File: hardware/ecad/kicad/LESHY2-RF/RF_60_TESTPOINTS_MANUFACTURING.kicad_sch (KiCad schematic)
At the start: 0 parts

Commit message: complete exact H2.3.13 RF testpoint sheet
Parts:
- added TP1: TP_PACK_FIXTURE_3V3, TestPoint:TestPoint_Pad_D1.0mm, symbol Leshy2:RF60_TP_PACK_FIXTURE_3V3
- added TP10: TP_EVIDENCE_MASK_INT_N, TestPoint:TestPoint_Pad_D1.0mm, symbol Leshy2:RF60_TP_EVIDENCE_MASK_INT_N
- added TP11: TP_SAFETY_UART_TX, TestPoint:TestPoint_Pad_D1.0mm, symbol Leshy2:RF60_TP_SAFETY_UART_TX
- added TP12: TP_SAFETY_UART_RX, TestPoint:TestPoint_Pad_D1.0mm, symbol Leshy2:RF60_TP_SAFETY_UART_RX
- added TP13: TP_SAFETY_SWDIO, TestPoint:TestPoint_Pad_D1.0mm, symbol Leshy2:RF60_TP_SAFETY_SWDIO
- added TP14: TP_SAFETY_SWCLK, TestPoint:TestPoint_Pad_D1.0mm, symbol Leshy2:RF60_TP_SAFETY_SWCLK
- added TP15: TP_SAFETY_NRST, TestPoint:TestPoint_Pad_D1.0mm, symbol Leshy2:RF60_TP_SAFETY_NRST
- added TP16: TP_EV_N2, TestPoint:TestPoint_Pad_D1.0mm, symbol Leshy2:RF60_TP_EV_N2
- added TP17: TP_EV_N3, TestPoint:TestPoint_Pad_D1.0mm, symbol Leshy2:RF60_TP_EV_N3
- added TP18: TP_EV_N4, TestPoint:TestPoint_Pad_D1.0mm, symbol Leshy2:RF60_TP_EV_N4
- added TP19: TP_EV_N5, TestPoint:TestPoint_Pad_D1.0mm, symbol Leshy2:RF60_TP_EV_N5
- added TP2: TP_PACK_UART_TX, TestPoint:TestPoint_Pad_D1.0mm, symbol Leshy2:RF60_TP_PACK_UART_TX
- added TP20: TP_EV_N6, TestPoint:TestPoint_Pad_D1.0mm, symbol Leshy2:RF60_TP_EV_N6
- added TP21: TP_EV_N8, TestPoint:TestPoint_Pad_D1.0mm, symbol Leshy2:RF60_TP_EV_N8
- added TP22: TP_ANY_TX_AON_N, TestPoint:TestPoint_Pad_D1.0mm, symbol Leshy2:RF60_TP_ANY_TX_AON_N
- added TP23: TP_POWER_TEMP, TestPoint:TestPoint_Pad_D1.0mm, symbol Leshy2:RF60_TP_POWER_TEMP
- added TP24: TP_RF_TEMP, TestPoint:TestPoint_Pad_D1.0mm, symbol Leshy2:RF60_TP_RF_TEMP
- added TP25: TP_RP_RESET_N, TestPoint:TestPoint_Pad_D1.0mm, symbol Leshy2:RF60_TP_RP_RESET_N
- added TP26: TP_RUN_PERMIT, TestPoint:TestPoint_Pad_D1.0mm, symbol Leshy2:RF60_TP_RUN_PERMIT
- added TP27: TP_POWER_FAULT_N, TestPoint:TestPoint_Pad_D1.0mm, symbol Leshy2:RF60_TP_POWER_FAULT_N
- added TP28: TP_POWER_GROUND, TestPoint:TestPoint_Pad_D1.0mm, symbol Leshy2:RF60_TP_POWER_GROUND
- added TP29: TP_AON_SAFE_3V3, TestPoint:TestPoint_Pad_D1.0mm, symbol Leshy2:RF60_TP_AON_SAFE_3V3
- added TP3: TP_PACK_UART_RX, TestPoint:TestPoint_Pad_D1.0mm, symbol Leshy2:RF60_TP_PACK_UART_RX
- added TP30: TP_3V3_MAIN, TestPoint:TestPoint_Pad_D1.0mm, symbol Leshy2:RF60_TP_3V3_MAIN
- added TP4: TP_PACK_SWDIO, TestPoint:TestPoint_Pad_D1.0mm, symbol Leshy2:RF60_TP_PACK_SWDIO
- added TP5: TP_PACK_SWCLK, TestPoint:TestPoint_Pad_D1.0mm, symbol Leshy2:RF60_TP_PACK_SWCLK
- added TP6: TP_PACK_NRST, TestPoint:TestPoint_Pad_D1.0mm, symbol Leshy2:RF60_TP_PACK_NRST
- added TP7: TP_MAIN_RAW_PG_N, TestPoint:TestPoint_Pad_D1.0mm, symbol Leshy2:RF60_TP_MAIN_RAW_PG_N
- added TP8: TP_VOICE_UPDATE, TestPoint:TestPoint_Pad_D1.0mm, symbol Leshy2:RF60_TP_VOICE_UPDATE
- added TP9: TP_VOICE_RAW_PG_N, TestPoint:TestPoint_Pad_D1.0mm, symbol Leshy2:RF60_TP_VOICE_RAW_PG_N
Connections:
- new net 3V3_MAIN: TP30.1 (TEST)
- new net ANY_TX_AON_N: TP22.1 (TEST)
- new net AON_SAFE_3V3: TP29.1 (TEST)
- new net EVIDENCE_MASK_INT_N_TP: TP10.1 (TEST)
- new net EV_N2_NRF0: TP16.1 (TEST)
- new net EV_N3_NRF1: TP17.1 (TEST)
- new net EV_N4_NRF2: TP18.1 (TEST)
- new net EV_N5_CC: TP19.1 (TEST)
- new net EV_N6_VOICE: TP20.1 (TEST)
- new net EV_N8_LORA_EXT: TP21.1 (TEST)
- new net MAIN_RAW_3V3_PG_N: TP7.1 (TEST)
- new net PACK_ADMISSION_NRST_N: TP6.1 (TEST)
- new net PACK_ADMISSION_SWCLK: TP5.1 (TEST)
- new net PACK_ADMISSION_SWDIO: TP4.1 (TEST)
- new net PACK_ADMISSION_UART_RX: TP3.1 (TEST)
- new net PACK_ADMISSION_UART_TX: TP2.1 (TEST)
- new net PACK_FIXTURE_3V3: TP1.1 (TEST)
- new net POWER_FAULT_N: TP27.1 (TEST)
- new net POWER_GROUND: TP28.1 (TEST)
- new net POWER_ZONE_TEMP_ADC: TP23.1 (TEST)
- new net RF_ZONE_TEMP_ADC: TP24.1 (TEST)
- new net RP_RESET_N: TP25.1 (TEST)
- new net RUN_PERMIT: TP26.1 (TEST)
- new net SAFETY_CONTROLLER_NRST_N: TP15.1 (TEST)
- new net SAFETY_SERVICE_UART_RX: TP12.1 (TEST)
- new net SAFETY_SERVICE_UART_TX: TP11.1 (TEST)
- new net SAFETY_SWCLK: TP14.1 (TEST)
- new net SAFETY_SWDIO: TP13.1 (TEST)
- new net VOICE_RAW_4V_PG_N: TP9.1 (TEST)
- new net VOICE_UPDATE_FIXTURE: TP8.1 (TEST)
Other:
- title: (none) -> Leshy2 — exact RF/power manufacturing and diagnostic test pads

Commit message: complete H2 schematic review package
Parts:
- added TP60007: TP_SYS_I2C_SDA, TestPoint:TestPoint_Pad_D1.0mm, symbol Leshy2:RF60_TP_SYS_I2C_SDA
- added TP60008: TP_SYS_I2C_SCL, TestPoint:TestPoint_Pad_D1.0mm, symbol Leshy2:RF60_TP_SYS_I2C_SCL
- added TP60009: TP_SYS_INT_N, TestPoint:TestPoint_Pad_D1.0mm, symbol Leshy2:RF60_TP_SYS_INT_N
- added TP60010: TP_PD_LOCAL_I2C_SDA, TestPoint:TestPoint_Pad_D1.0mm, symbol Leshy2:RF60_TP_PD_LOCAL_I2C_SDA
- added TP60011: TP_PD_LOCAL_I2C_SCL, TestPoint:TestPoint_Pad_D1.0mm, symbol Leshy2:RF60_TP_PD_LOCAL_I2C_SCL
- added TP60012: TP_PD_EEPROM_WP, TestPoint:TestPoint_Pad_D1.0mm, symbol Leshy2:RF60_TP_PD_EEPROM_WP
- added TP60013: TP_RP_SERVICE_VBUS_SENSE, TestPoint:TestPoint_Pad_D1.0mm, symbol Leshy2:RF60_TP_RP_SERVICE_VBUS_SENSE
- added TP60038: TP_RUN_LOOP_RAW, TestPoint:TestPoint_Pad_D1.0mm, symbol Leshy2:RF60_TP_RUN_LOOP_RAW
- added TP60039: TP_RUN_EDGE, TestPoint:TestPoint_Pad_D1.0mm, symbol Leshy2:RF60_TP_RUN_EDGE
- added TP60040: TP_FAULT_ASSERT_N, TestPoint:TestPoint_Pad_D1.0mm, symbol Leshy2:RF60_TP_FAULT_ASSERT_N
- added TP60041: TP_WDI, TestPoint:TestPoint_Pad_D1.0mm, symbol Leshy2:RF60_TP_WDI
- added TP60042: TP_POR_N, TestPoint:TestPoint_Pad_D1.0mm, symbol Leshy2:RF60_TP_POR_N
- added TP60043: TP_FAULT_LATCH_SENSE_AON, TestPoint:TestPoint_Pad_D1.0mm, symbol Leshy2:RF60_TP_FAULT_LATCH_SENSE_AON
- added TP60044: TP_NRF0_CE_SAFE, TestPoint:TestPoint_Pad_D1.0mm, symbol Leshy2:RF60_TP_NRF0_CE_SAFE
- added TP60045: TP_NRF1_CE_SAFE, TestPoint:TestPoint_Pad_D1.0mm, symbol Leshy2:RF60_TP_NRF1_CE_SAFE
- added TP60046: TP_NRF2_CE_SAFE, TestPoint:TestPoint_Pad_D1.0mm, symbol Leshy2:RF60_TP_NRF2_CE_SAFE
- added TP60047: TP_NRF_RAIL_EN_SAFE, TestPoint:TestPoint_Pad_D1.0mm, symbol Leshy2:RF60_TP_NRF_RAIL_EN_SAFE
- added TP60048: TP_CC_RAIL_EN_SAFE, TestPoint:TestPoint_Pad_D1.0mm, symbol Leshy2:RF60_TP_CC_RAIL_EN_SAFE
- added TP60049: TP_VOICE_RAIL_EN_SAFE, TestPoint:TestPoint_Pad_D1.0mm, symbol Leshy2:RF60_TP_VOICE_RAIL_EN_SAFE
- added TP60050: TP_VOICE_PTT_SAFE_N, TestPoint:TestPoint_Pad_D1.0mm, symbol Leshy2:RF60_TP_VOICE_PTT_SAFE_N
- added TP60051: TP_EXT_5V_EN_SAFE, TestPoint:TestPoint_Pad_D1.0mm, symbol Leshy2:RF60_TP_EXT_5V_EN_SAFE
- added TP60052: TP_RP_ANY_TX_N, TestPoint:TestPoint_Pad_D1.0mm, symbol Leshy2:RF60_TP_RP_ANY_TX_N
- renumbered TP1 to TP60001, TP2 to TP60002, TP3 to TP60003, TP4 to TP60004, TP5 to TP60005, TP6 to TP60006, TP7 to TP60014, TP8 to TP60015, TP9 to TP60016, TP10 to TP60017, TP11 to TP60018, TP12 to TP60019, TP13 to TP60020, TP14 to TP60021, TP15 to TP60022, TP16 to TP60023, TP17 to TP60024, TP18 to TP60025, TP19 to TP60026, TP20 to TP60027, TP21 to TP60028, TP22 to TP60029, TP23 to TP60030, TP24 to TP60031, TP25 to TP60032, TP26 to TP60033, TP27 to TP60034, TP28 to TP60035, TP29 to TP60036, TP30 to TP60037
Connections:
- new net CC_PWR_EN_SAFE: TP60048.1 (TEST)
- new net EXT_ANY_5V_EN_SAFE: TP60051.1 (TEST)
- new net FAULT_ASSERT_N: TP60040.1 (TEST)
- new net FAULT_LATCH_SENSE_AON: TP60043.1 (TEST)
- new net NRF0_CE_SAFE: TP60044.1 (TEST)
- new net NRF1_CE_SAFE: TP60045.1 (TEST)
- new net NRF2_CE_SAFE: TP60046.1 (TEST)
- new net NRF_GROUP_PWR_EN_SAFE: TP60047.1 (TEST)
- new net PD_EEPROM_WP: TP60012.1 (TEST)
- new net PD_LOCAL_I2C_SCL: TP60011.1 (TEST)
- new net PD_LOCAL_I2C_SDA: TP60010.1 (TEST)
- new net POR_N: TP60042.1 (TEST)
- new net RP_ANY_TX_N: TP60052.1 (TEST)
- new net RP_SERVICE_VBUS_SENSE_ONLY: TP60013.1 (TEST)
- new net RUN_EDGE: TP60039.1 (TEST)
- new net RUN_LOOP_RAW: TP60038.1 (TEST)
- new net SAFETY_WATCHDOG_WDI: TP60041.1 (TEST)
- new net SYS_I2C_SCL: TP60008.1 (TEST)
- new net SYS_I2C_SDA: TP60007.1 (TEST)
- new net SYS_INT_N: TP60009.1 (TEST)
- new net VOICE_DOMAIN_EN_SAFE: TP60049.1 (TEST)
- new net VOICE_PTT_SAFE_N: TP60050.1 (TEST)
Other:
- moved on the sheet: TP60014, TP60015, TP60016, TP60017, TP60018, TP60019, TP60020, TP60021, TP60022, TP60023, TP60024, TP60025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

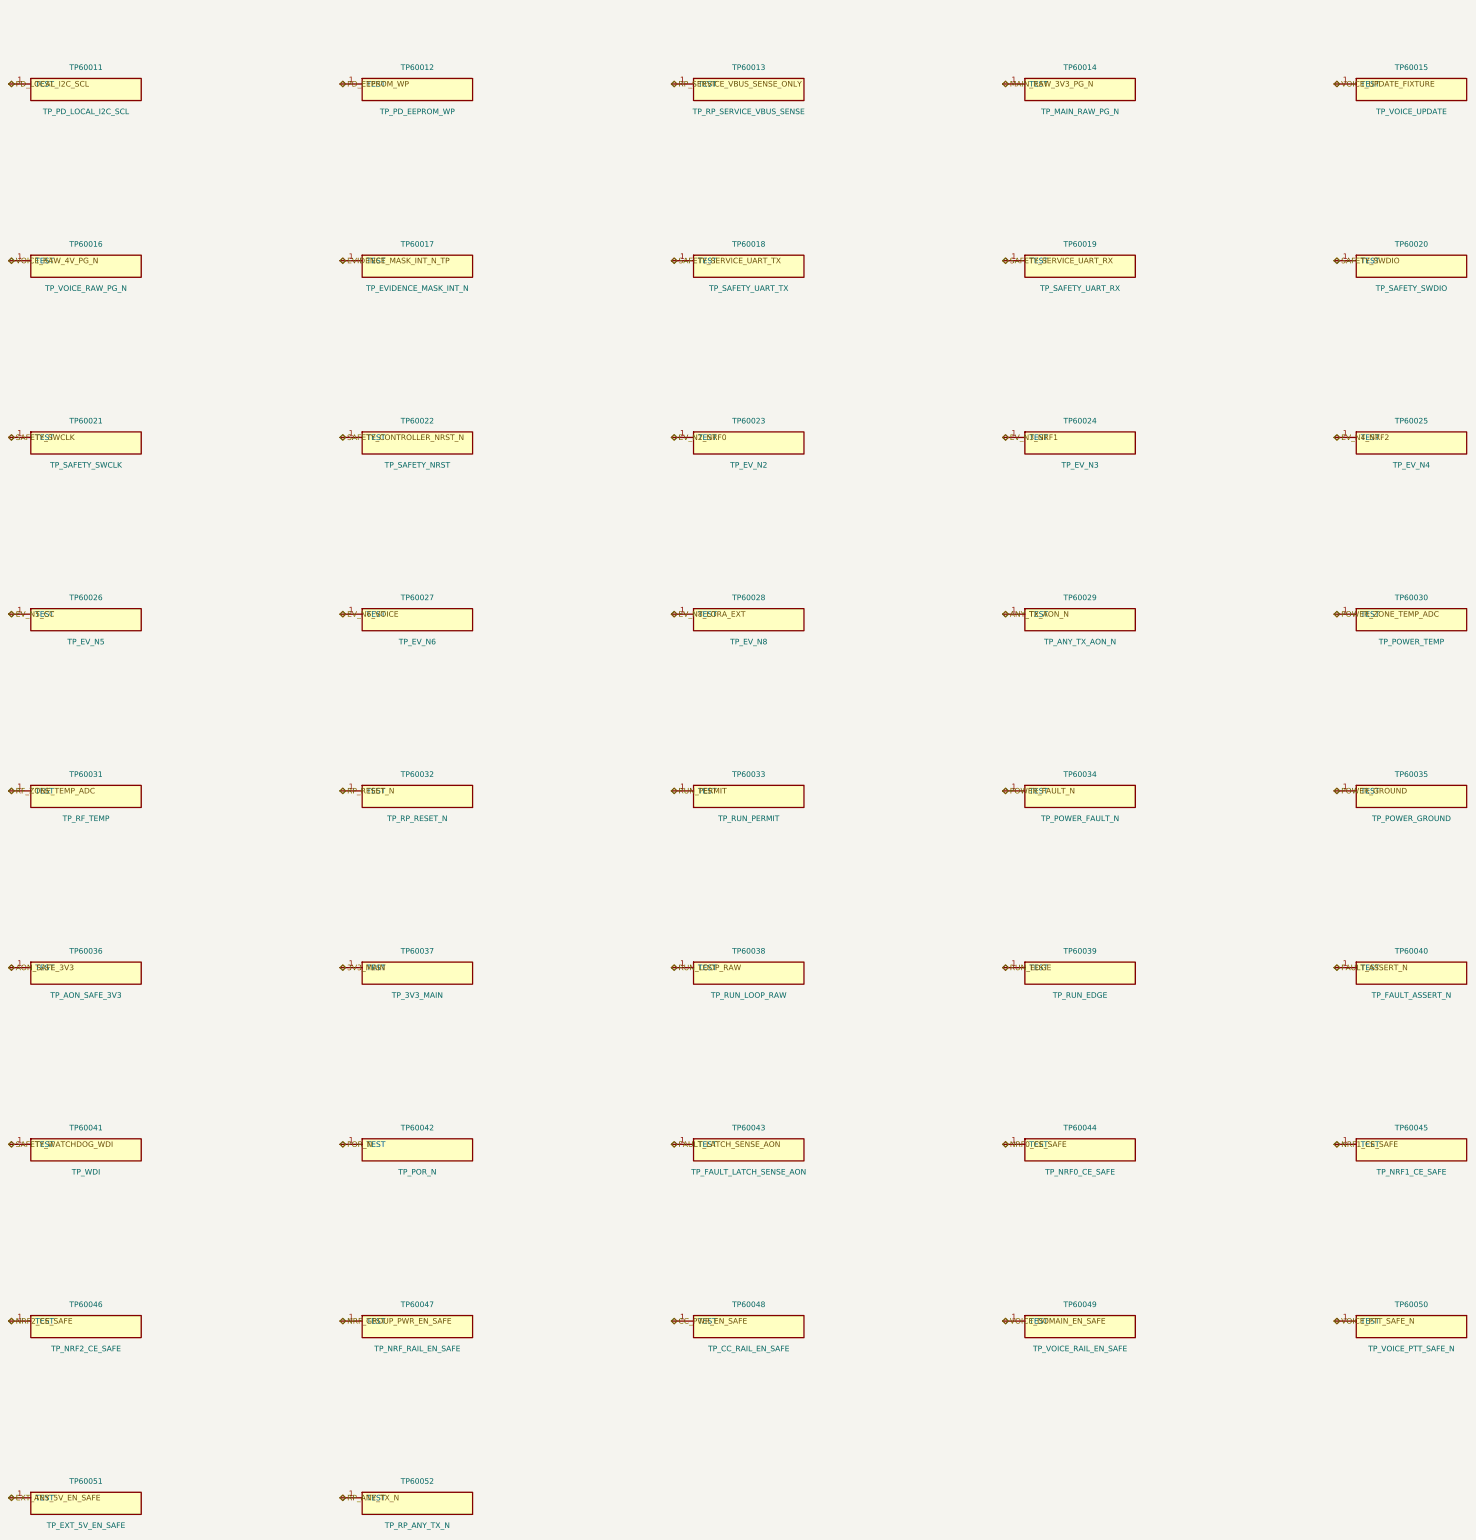
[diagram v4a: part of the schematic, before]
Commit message: Reclose H2 through H4 on dual SA818S architecture
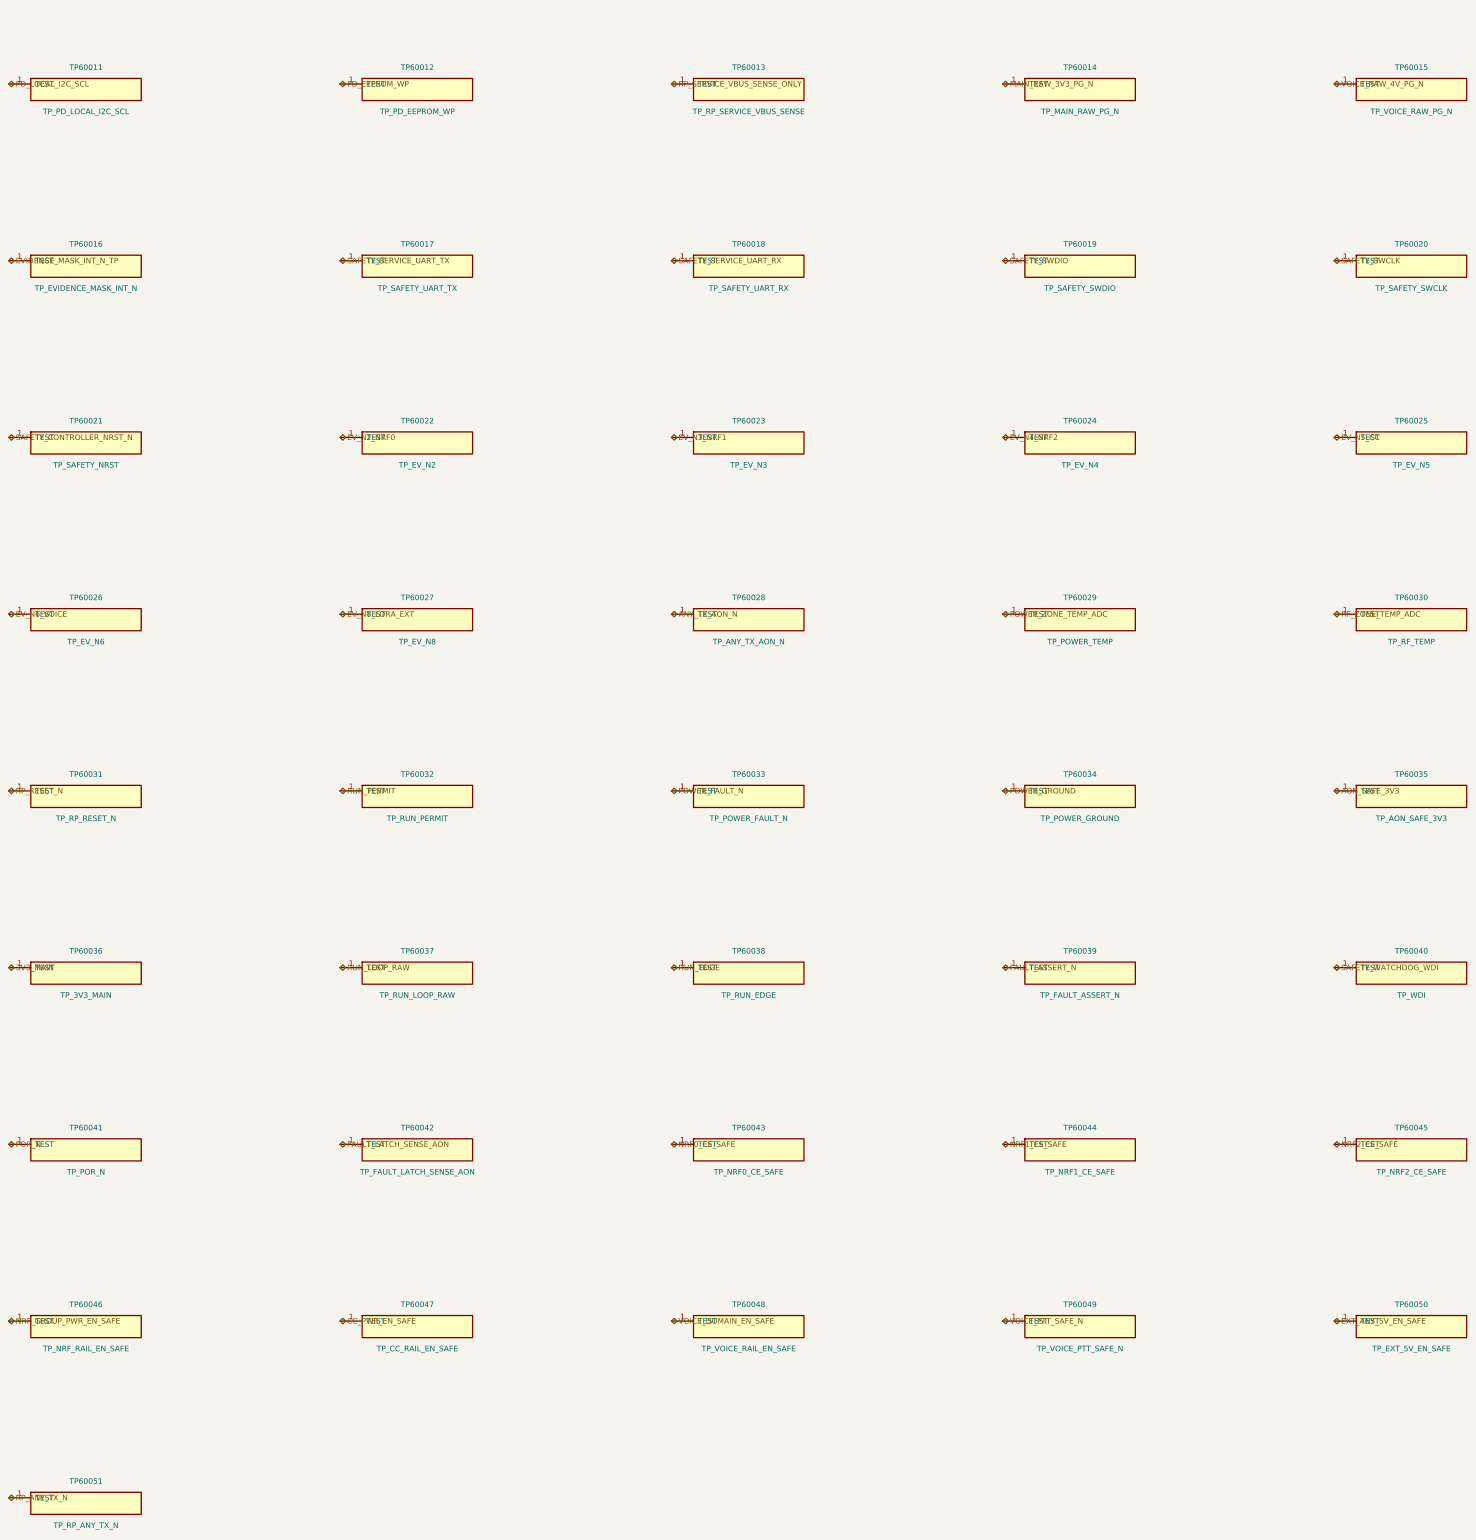
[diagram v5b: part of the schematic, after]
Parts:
- removed TP60015: TP_VOICE_UPDATE, TestPoint:TestPoint_Pad_D1.0mm, symbol Leshy2:RF60_TP_VOICE_UPDATE
- renumbered TP60016 to TP60015, TP60017 to TP60016, TP60018 to TP60017, TP60019 to TP60018, TP60020 to TP60019, TP60021 to TP60020, TP60022 to TP60021, TP60023 to TP60022, TP60024 to TP60023, TP60025 to TP60024, TP60026 to TP60025, TP60027 to TP60026, TP60028 to TP60027, TP60029 to TP60028, TP60030 to TP60029, TP60031 to TP60030, TP60032 to TP60031, TP60033 to TP60032, TP60034 to TP60033, TP60035 to TP60034, TP60036 to TP60035, TP60037 to TP60036, TP60038 to TP60037, TP60039 to TP60038, TP60040 to TP60039, TP60041 to TP60040, TP60042 to TP60041, TP60043 to TP60042, TP60044 to TP60043, TP60045 to TP60044, TP60046 to TP60045, TP60047 to TP60046, TP60048 to TP60047, TP60049 to TP60048, TP60050 to TP60049, TP60051 to TP60050, TP60052 to TP60051
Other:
- moved on the sheet: TP60015, TP60016, TP60017, TP60018, TP60019, TP60020, TP60021, TP60022, TP60023, TP60024, TP60025, TP60026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
